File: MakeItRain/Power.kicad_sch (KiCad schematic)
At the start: 12 parts, among them IC4 LM2597MX-5.0_NOPB, P1 Screw_Terminal_01x02, Q1 IRF9Z34NPBF, U1 178.6165.0001

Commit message: wip for input fix.
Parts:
- R19: renamed from R1; footprint Resistor_THT:R_Axial_DIN0207_L6.3mm_D2.5mm_P5.08mm_Vertical -> Resistor_THT:R_Axial_DIN0207_L6.3mm_D2.5mm_P2.54mm_Vertical
- R20: renamed from R6; footprint Resistor_THT:R_Axial_DIN0207_L6.3mm_D2.5mm_P5.08mm_Vertical -> Resistor_THT:R_Axial_DIN0207_L6.3mm_D2.5mm_P2.54mm_Vertical
- renumbered C1 to C6, C2 to C7, C3 to C8, C4 to C9, D1 to D9, IC4 to IC2, Q1 to Q13, U1 to U2
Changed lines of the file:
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@@
   (symbol (lib_id "Device:CP1") (at 200.66 54.61 0) (unit 1)
     (in_bom yes) (on_board yes)
-    (property "Reference" "C3" (id 0) (at 203.581 53.4416 0)
+    (property "Reference" "C8" (id 0) (at 203.581 53.4416 0)
       (effects (font (size 1.27 1.27)) (justify left))
     )
@@
   (symbol (lib_id "power:GND") (at 48.26 68.58 0) (unit 1)
     (in_bom yes) (on_board yes)
-    (property "Reference" "#PWR01" (id 0) (at 48.26 74.93 0)
+    (property "Reference" "#PWR031" (id 0) (at 48.26 74.93 0)
       (effects (font (size 1.27 1.27)) hide)
     )
@@
   (symbol (lib_id "SamacSys_Parts:LM2597MX-5.0_NOPB") (at 134.62 48.26 0) (unit 1)
     (in_bom yes) (on_board yes)
-    (property "Reference" "IC4" (id 0) (at 163.83 41.529 0))
+    (property "Reference" "IC2" (id 0) (at 163.83 41.529 0))
     (property "Value" "LM2597MX-5.0_NOPB" (id 1) (at 163.83 43.8404 0))
     (property "Footprint" "SamacSys_Parts:SOIC127P600X175-8N" (id 2) (at 189.23 45.72 0)
@@
   (symbol (lib_id "power:+VDC") (at 200.66 50.8 270) (mirror x) (unit 1)
     (in_bom yes) (on_board yes)
-    (property "Reference" "#PWR025" (id 0) (at 198.12 50.8 0)
+    (property "Reference" "#PWR037" (id 0) (at 198.12 50.8 0)
       (effects (font (size 1.27 1.27)) hide)
     )
@@
   (symbol (lib_id "Device:C") (at 193.04 59.69 0) (unit 1)
     (in_bom yes) (on_board yes)
-    (property "Reference" "C2" (id 0) (at 195.961 58.5216 0)
+    (property "Reference" "C7" (id 0) (at 195.961 58.5216 0)
       (effects (font (size 1.27 1.27)) (justify left))
     )
@@
   (symbol (lib_id "Device:R") (at 64.77 73.66 0) (unit 1)
     (in_bom yes) (on_board yes)
-    (property "Reference" "R1" (id 0) (at 66.548 72.4916 0)
+    (property "Reference" "R19" (id 0) (at 66.548 72.4916 0)
       (effects (font (size 1.27 1.27)) (justify left))
     )
@@
       (effects (font (size 1.27 1.27)) (justify left))
     )
-    (property "Footprint" "Resistor_THT:R_Axial_DIN0207_L6.3mm_D2.5mm_P5.08mm_Vertical" (id 2) (at 62.992 73.66 90)
+    (property "Footprint" "Resistor_THT:R_Axial_DIN0207_L6.3mm_D2.5mm_P2.54mm_Vertical" (id 2) (at 62.992 73.66 90)
       (effects (font (size 1.27 1.27)) hide)
     )
@@
   (symbol (lib_id "power:+VDC") (at 95.25 35.56 0) (unit 1)
     (in_bom yes) (on_board yes)
-    (property "Reference" "#PWR09" (id 0) (at 95.25 38.1 0)
+    (property "Reference" "#PWR033" (id 0) (at 95.25 38.1 0)
       (effects (font (size 1.27 1.27)) hide)
     )
@@
   (symbol (lib_id "Diode:1N5817") (at 209.55 54.61 90) (mirror x) (unit 1)
     (in_bom yes) (on_board yes)
-    (property "Reference" "D1" (id 0) (at 211.582 53.4416 90)
+    (property "Reference" "D9" (id 0) (at 211.582 53.4416 90)
       (effects (font (size 1.27 1.27)) (justify right))
     )
@@
   (symbol (lib_id "power:+5V") (at 217.17 35.56 0) (unit 1)
     (in_bom yes) (on_board yes)
-    (property "Reference" "#PWR026" (id 0) (at 217.17 39.37 0)
+    (property "Reference" "#PWR038" (id 0) (at 217.17 39.37 0)
       (effects (font (size 1.27 1.27)) hide)
     )
@@
   (symbol (lib_id "power:GND") (at 121.92 59.69 0) (unit 1)
     (in_bom yes) (on_board yes)
-    (property "Reference" "#PWR017" (id 0) (at 121.92 66.04 0)
+    (property "Reference" "#PWR035" (id 0) (at 121.92 66.04 0)
       (effects (font (size 1.27 1.27)) hide)
     )
@@
   (symbol (lib_id "SamacSys_Parts:IRF9Z34NPBF") (at 64.77 67.31 270) (mirror x) (unit 1)
     (in_bom yes) (on_board yes)
-    (property "Reference" "Q1" (id 0) (at 68.4784 56.388 0)
+    (property "Reference" "Q13" (id 0) (at 68.4784 56.388 0)
       (effects (font (size 1.27 1.27)) (justify left))
     )
@@
   (symbol (lib_id "power:GND") (at 64.77 81.28 0) (unit 1)
     (in_bom yes) (on_board yes)
-    (property "Reference" "#PWR06" (id 0) (at 64.77 87.63 0)
+    (property "Reference" "#PWR032" (id 0) (at 64.77 87.63 0)
       (effects (font (size 1.27 1.27)) hide)
     )
@@
   (symbol (lib_id "Device:C") (at 121.92 54.61 0) (unit 1)
     (in_bom yes) (on_board yes)
-    (property "Reference" "C1" (id 0) (at 124.841 53.4416 0)
+    (property "Reference" "C6" (id 0) (at 124.841 53.4416 0)
       (effects (font (size 1.27 1.27)) (justify left))
     )
@@
   (symbol (lib_id "Device:R") (at 110.49 44.45 0) (unit 1)
     (in_bom yes) (on_board yes)
-    (property "Reference" "R6" (id 0) (at 112.268 43.2816 0)
+    (property "Reference" "R20" (id 0) (at 112.268 43.2816 0)
       (effects (font (size 1.27 1.27)) (justify left))
     )
@@
       (effects (font (size 1.27 1.27)) (justify left))
     )
-    (property "Footprint" "Resistor_THT:R_Axial_DIN0207_L6.3mm_D2.5mm_P5.08mm_Vertical" (id 2) (at 108.712 44.45 90)
+    (property "Footprint" "Resistor_THT:R_Axial_DIN0207_L6.3mm_D2.5mm_P2.54mm_Vertical" (id 2) (at 108.712 44.45 90)
       (effects (font (size 1.27 1.27)) hide)
     )
@@
   (symbol (lib_id "power:GND") (at 196.85 64.77 0) (unit 1)
     (in_bom yes) (on_board yes)
-    (property "Reference" "#PWR024" (id 0) (at 196.85 71.12 0)
+    (property "Reference" "#PWR036" (id 0) (at 196.85 71.12 0)
       (effects (font (size 1.27 1.27)) hide)
     )
@@
   (symbol (lib_id "Device:CP1") (at 220.98 52.07 0) (unit 1)
     (in_bom yes) (on_board yes)
-    (property "Reference" "C4" (id 0) (at 223.901 50.9016 0)
+    (property "Reference" "C9" (id 0) (at 223.901 50.9016 0)
       (effects (font (size 1.27 1.27)) (justify left))
     )
@@
   (symbol (lib_id "SamacSys_Parts:178.6165.0001") (at 74.93 44.45 0) (unit 1)
     (in_bom yes) (on_board yes)
-    (property "Reference" "U1" (id 0) (at 85.09 37.719 0))
+    (property "Reference" "U2" (id 0) (at 85.09 37.719 0))
     (property "Value" "178.6165.0001" (id 1) (at 85.09 40.0304 0))
     (property "Footprint" "SamacSys_Parts:17861650001" (id 2) (at 91.44 41.91 0)
@@
   (symbol (lib_id "power:+VDC") (at 110.49 35.56 0) (unit 1)
     (in_bom yes) (on_board yes)
-    (property "Reference" "#PWR016" (id 0) (at 110.49 38.1 0)
-      (effects (font (size 1.27 1.27)) hide)
-    )
+    (property "Reference" "#PWR034" (id 0) (at 110.49 38.1 0)
+      (effects (font (size 1.27 1.27)) hide)
+    )

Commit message: wip for layout
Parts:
- renumbered D9 to D10, R19 to R21, R20 to R22
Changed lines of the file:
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@@
   (symbol (lib_id "power:GND") (at 48.26 68.58 0) (unit 1)
     (in_bom yes) (on_board yes)
-    (property "Reference" "#PWR031" (id 0) (at 48.26 74.93 0)
+    (property "Reference" "#PWR034" (id 0) (at 48.26 74.93 0)
       (effects (font (size 1.27 1.27)) hide)
     )
@@
   (symbol (lib_id "power:+VDC") (at 200.66 50.8 270) (mirror x) (unit 1)
     (in_bom yes) (on_board yes)
-    (property "Reference" "#PWR037" (id 0) (at 198.12 50.8 0)
+    (property "Reference" "#PWR040" (id 0) (at 198.12 50.8 0)
       (effects (font (size 1.27 1.27)) hide)
     )
@@
   (symbol (lib_id "Device:R") (at 64.77 73.66 0) (unit 1)
     (in_bom yes) (on_board yes)
-    (property "Reference" "R19" (id 0) (at 66.548 72.4916 0)
+    (property "Reference" "R21" (id 0) (at 66.548 72.4916 0)
       (effects (font (size 1.27 1.27)) (justify left))
     )
@@
   (symbol (lib_id "power:+VDC") (at 95.25 35.56 0) (unit 1)
     (in_bom yes) (on_board yes)
-    (property "Reference" "#PWR033" (id 0) (at 95.25 38.1 0)
+    (property "Reference" "#PWR036" (id 0) (at 95.25 38.1 0)
       (effects (font (size 1.27 1.27)) hide)
     )
@@
   (symbol (lib_id "Diode:1N5817") (at 209.55 54.61 90) (mirror x) (unit 1)
     (in_bom yes) (on_board yes)
-    (property "Reference" "D9" (id 0) (at 211.582 53.4416 90)
+    (property "Reference" "D10" (id 0) (at 211.582 53.4416 90)
       (effects (font (size 1.27 1.27)) (justify right))
     )
@@
   (symbol (lib_id "power:+5V") (at 217.17 35.56 0) (unit 1)
     (in_bom yes) (on_board yes)
-    (property "Reference" "#PWR038" (id 0) (at 217.17 39.37 0)
+    (property "Reference" "#PWR041" (id 0) (at 217.17 39.37 0)
       (effects (font (size 1.27 1.27)) hide)
     )
@@
   (symbol (lib_id "power:GND") (at 121.92 59.69 0) (unit 1)
     (in_bom yes) (on_board yes)
-    (property "Reference" "#PWR035" (id 0) (at 121.92 66.04 0)
+    (property "Reference" "#PWR038" (id 0) (at 121.92 66.04 0)
       (effects (font (size 1.27 1.27)) hide)
     )
@@
   (symbol (lib_id "power:GND") (at 64.77 81.28 0) (unit 1)
     (in_bom yes) (on_board yes)
-    (property "Reference" "#PWR032" (id 0) (at 64.77 87.63 0)
+    (property "Reference" "#PWR035" (id 0) (at 64.77 87.63 0)
       (effects (font (size 1.27 1.27)) hide)
     )
@@
   (symbol (lib_id "Device:R") (at 110.49 44.45 0) (unit 1)
     (in_bom yes) (on_board yes)
-    (property "Reference" "R20" (id 0) (at 112.268 43.2816 0)
+    (property "Reference" "R22" (id 0) (at 112.268 43.2816 0)
       (effects (font (size 1.27 1.27)) (justify left))
     )
@@
   (symbol (lib_id "power:GND") (at 196.85 64.77 0) (unit 1)
     (in_bom yes) (on_board yes)
-    (property "Reference" "#PWR036" (id 0) (at 196.85 71.12 0)
+    (property "Reference" "#PWR039" (id 0) (at 196.85 71.12 0)
       (effects (font (size 1.27 1.27)) hide)
     )
@@
   (symbol (lib_id "power:+VDC") (at 110.49 35.56 0) (unit 1)
     (in_bom yes) (on_board yes)
-    (property "Reference" "#PWR034" (id 0) (at 110.49 38.1 0)
-      (effects (font (size 1.27 1.27)) hide)
-    )
+    (property "Reference" "#PWR037" (id 0) (at 110.49 38.1 0)
+      (effects (font (size 1.27 1.27)) hide)
+    )

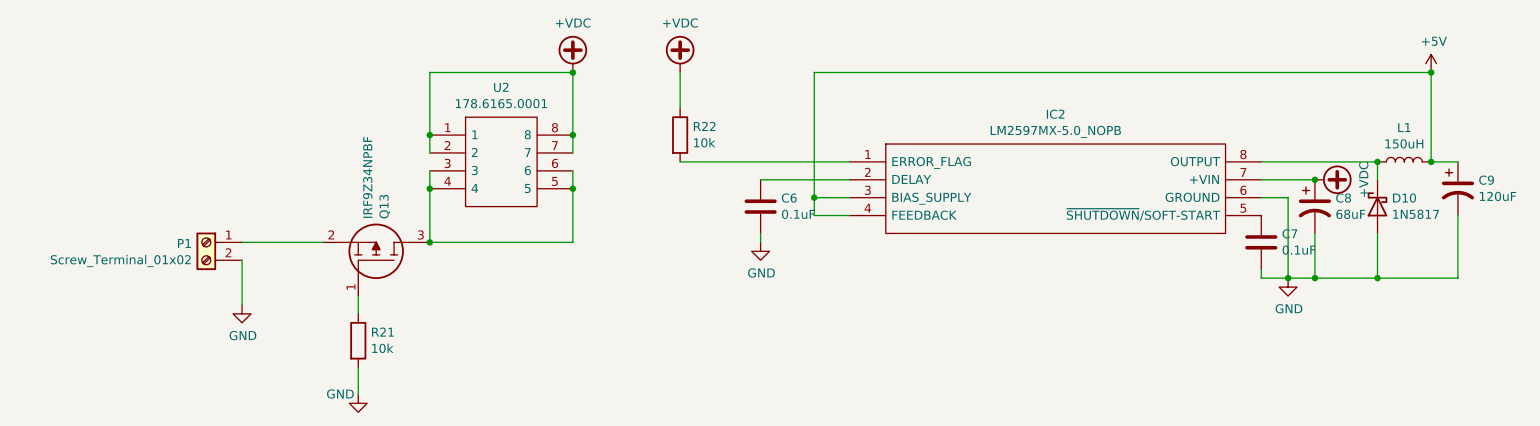
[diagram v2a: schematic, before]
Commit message: due to lack of chips (LM2597) i'm switching (no pun intended) to having the power system be a daughter board that can be plugged in once i find some replacements.
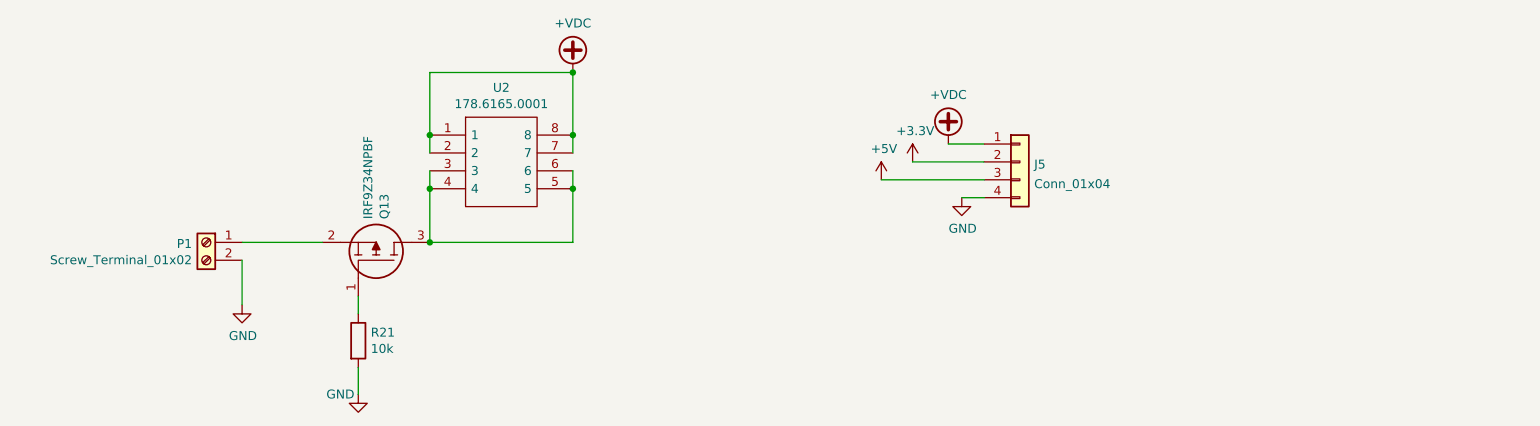
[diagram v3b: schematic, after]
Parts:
- removed C6, C7: 0.1uF, Capacitor_THT:C_Disc_D4.7mm_W2.5mm_P5.00mm, symbol Device:C
- removed C8: 68uF, Capacitor_THT:CP_Radial_D8.0mm_P3.50mm, symbol Device:CP1
- removed C9: 120uF, Capacitor_THT:CP_Radial_D8.0mm_P3.50mm, symbol Device:CP1
- removed D10: 1N5817, Diode_THT:D_DO-41_SOD81_P10.16mm_Horizontal, symbol Diode:1N5817
- removed IC2: LM2597MX-5.0_NOPB, SamacSys_Parts:SOIC127P600X175-8N, symbol SamacSys_Parts:LM2597MX-5.0_NOPB
- removed L1: 150uH, Inductor_THT:L_Axial_L6.6mm_D2.7mm_P10.16mm_Horizontal_Vishay_IM-2, symbol Device:L
- removed R22: 10k, Resistor_THT:R_Axial_DIN0207_L6.3mm_D2.5mm_P2.54mm_Vertical, symbol Device:R
- added J5: Conn_01x04, Connector_PinSocket_2.54mm:PinSocket_1x04_P2.54mm_Vertical, symbol Connector_Generic:Conn_01x04
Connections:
- net +5V: now also J5.3 (Pin_3)
- net +VDC: now also J5.1 (Pin_1)
- net GND: now also J5.4 (Pin_4)
- new net +3V3: J5.2 (Pin_2)

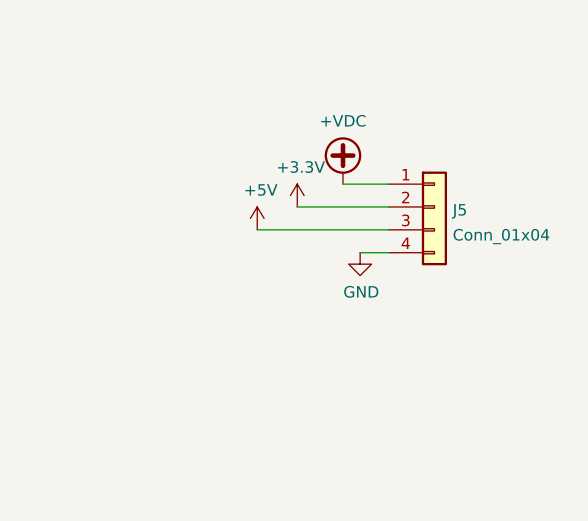
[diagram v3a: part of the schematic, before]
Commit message: removed the 5V on the baseboard and daughterboard plug.
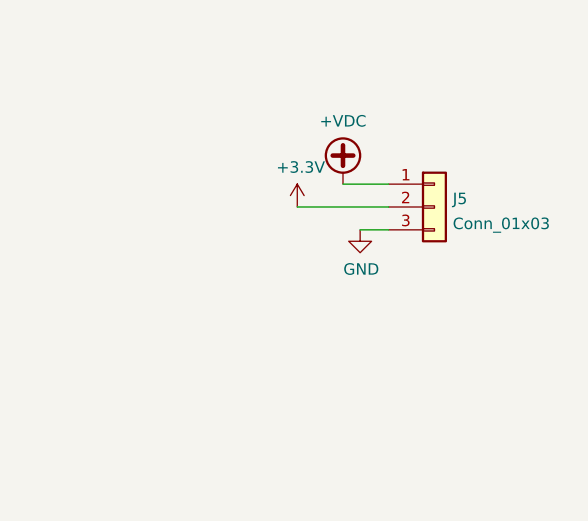
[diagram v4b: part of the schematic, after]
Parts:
- removed J5: Conn_01x04, Connector_PinSocket_2.54mm:PinSocket_1x04_P2.54mm_Vertical, symbol Connector_Generic:Conn_01x04
- added J5: Conn_01x03, Connector_PinHeader_2.54mm:PinHeader_1x03_P2.54mm_Vertical, symbol Connector_Generic:Conn_01x03
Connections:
- net +3V3: now also J5.2 (Pin_2)
- net +VDC: now also J5.1 (Pin_1)
- net GND: now also J5.3 (Pin_3)
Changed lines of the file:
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@@
     (stroke (width 0) (type default) (color 0 0 0 0))
   )
-  (wire (pts (xy 150.495 53.34) (xy 153.67 53.34))
+  (wire (pts (xy 150.495 50.8) (xy 153.67 50.8))
     (stroke (width 0) (type default) (color 0 0 0 0))
   )
@@
   )
   (wire (pts (xy 74.93 35.56) (xy 95.25 35.56))
-    (stroke (width 0) (type default) (color 0 0 0 0))
-  )
-  (wire (pts (xy 139.065 50.8) (xy 153.67 50.8))
     (stroke (width 0) (type default) (color 0 0 0 0))
   )
@@
     (pin "1")
   )
-  (symbol (lib_id "Connector_Generic:Conn_01x04") (at 158.75 48.26 0) (unit 1)
-    (in_bom yes) (on_board yes) (fields_autoplaced)
-    (property "Reference" "J5" (id 0) (at 160.782 48.6215 0)
-      (effects (font (size 1.27 1.27)) (justify left))
-    )
-    (property "Value" "Conn_01x04" (id 1) (at 160.782 51.3966 0)
-      (effects (font (size 1.27 1.27)) (justify left))
-    )
-    (property "Footprint" "Connector_PinSocket_2.54mm:PinSocket_1x04_P2.54mm_Vertical" (id 2) (at 158.75 48.26 0)
-      (effects (font (size 1.27 1.27)) hide)
-    )
-    (property "Datasheet" "~" (id 3) (at 158.75 48.26 0)
-      (effects (font (size 1.27 1.27)) hide)
-    )
-    (pin "1")
-    (pin "2")
-    (pin "3")
-    (pin "4")
-  )
-  (symbol (lib_id "power:+5V") (at 139.065 50.8 0) (unit 1)
-    (in_bom yes) (on_board yes)
-    (property "Reference" "#PWR02" (id 0) (at 139.065 54.61 0)
-      (effects (font (size 1.27 1.27)) hide)
-    )
-    (property "Value" "+5V" (id 1) (at 139.446 46.4058 0))
-    (property "Footprint" "" (id 2) (at 139.065 50.8 0)
-      (effects (font (size 1.27 1.27)) hide)
-    )
-    (property "Datasheet" "" (id 3) (at 139.065 50.8 0)
-      (effects (font (size 1.27 1.27)) hide)
-    )
-    (pin "1")
-  )
   (symbol (lib_id "power:GND") (at 64.77 81.28 0) (unit 1)
     (in_bom yes) (on_board yes)
@@
     (pin "2")
   )
-  (symbol (lib_id "power:GND") (at 150.495 53.34 0) (unit 1)
-    (in_bom yes) (on_board yes)
-    (property "Reference" "#PWR09" (id 0) (at 150.495 59.69 0)
-      (effects (font (size 1.27 1.27)) hide)
-    )
-    (property "Value" "GND" (id 1) (at 150.622 57.7342 0))
-    (property "Footprint" "" (id 2) (at 150.495 53.34 0)
-      (effects (font (size 1.27 1.27)) hide)
-    )
-    (property "Datasheet" "" (id 3) (at 150.495 53.34 0)
+  (symbol (lib_id "power:GND") (at 150.495 50.8 0) (unit 1)
+    (in_bom yes) (on_board yes)
+    (property "Reference" "#PWR09" (id 0) (at 150.495 57.15 0)
+      (effects (font (size 1.27 1.27)) hide)
+    )
+    (property "Value" "GND" (id 1) (at 150.622 55.1942 0))
+    (property "Footprint" "" (id 2) (at 150.495 50.8 0)
+      (effects (font (size 1.27 1.27)) hide)
+    )
+    (property "Datasheet" "" (id 3) (at 150.495 50.8 0)
       (effects (font (size 1.27 1.27)) hide)
     )
@@
     (pin "8")
   )
+  (symbol (lib_id "Connector_Generic:Conn_01x03") (at 158.75 48.26 0) (unit 1)
+    (in_bom yes) (on_board yes) (fields_autoplaced)
+    (property "Reference" "J5" (id 0) (at 160.782 47.3515 0)
+      (effects (font (size 1.27 1.27)) (justify left))
+    )
+    (property "Value" "Conn_01x03" (id 1) (at 160.782 50.1266 0)
+      (effects (font (size 1.27 1.27)) (justify left))
+    )
+    (property "Footprint" "Connector_PinHeader_2.54mm:PinHeader_1x03_P2.54mm_Vertical" (id 2) (at 158.75 48.26 0)
+      (effects (font (size 1.27 1.27)) hide)
+    )
+    (property "Datasheet" "~" (id 3) (at 158.75 48.26 0)
+      (effects (font (size 1.27 1.27)) hide)
+    )
+    (pin "1")
+    (pin "2")
+    (pin "3")
+  )
 )
